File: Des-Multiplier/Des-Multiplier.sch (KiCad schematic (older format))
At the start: 44 parts, among them SW1 SW_Push, U1 NE555P, U2 NE555P

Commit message: added state machine based timing control
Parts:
- added U?: 74LS175, symbol 74xx:74LS175
- added U? (x7): 74HC00, symbol 74xx:74HC00
- added U? (x6): 74LS00, symbol 74xx:74LS00
- C1, C2, C3, C4: symbol Device:C -> Des-Multiplier-rescue:C-Device
- D? (x8): symbol Device:LED -> Des-Multiplier-rescue:LED-Device
- R1, R2, R3, R4, R? (x16): symbol Device:R -> Des-Multiplier-rescue:R-Device
- SW1: symbol Switch:SW_Push -> Des-Multiplier-rescue:SW_Push-Switch
- SW? (x2): symbol Switch:SW_DIP_x04 -> Des-Multiplier-rescue:SW_DIP_x04-Switch
- U1, U2: symbol Timer:NE555P -> Des-Multiplier-rescue:NE555P-Timer
- U? (x3): symbol 74xx:74LS194 -> Des-Multiplier-rescue:74LS194-74xx
- U? (x2): symbol 74xx:74LS283 -> Des-Multiplier-rescue:74LS283-74xx
- U?: symbol 74xx:74LS244 -> Des-Multiplier-rescue:74LS244-74xx
- U?: symbol 74xx:74LS273 -> Des-Multiplier-rescue:74LS273-74xx
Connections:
- net labels added: AccCLK, Acc_Load_En, Load, PreState0, ResetFlag, State0, State1, State2, ~AccCLK, ~GoDetect, ~GoEdge, ~Load, ~Load~, ~Q1~nQ0, ~Q2~n~Q1~, ~Reset, ~ResetFlag, ~S2~nQ0, ~State0, ~State1, ~State2
- net labels removed: Astatus+CLK, Reset
- wire segments 129 -> 152
- no-connect marks 7 -> 8

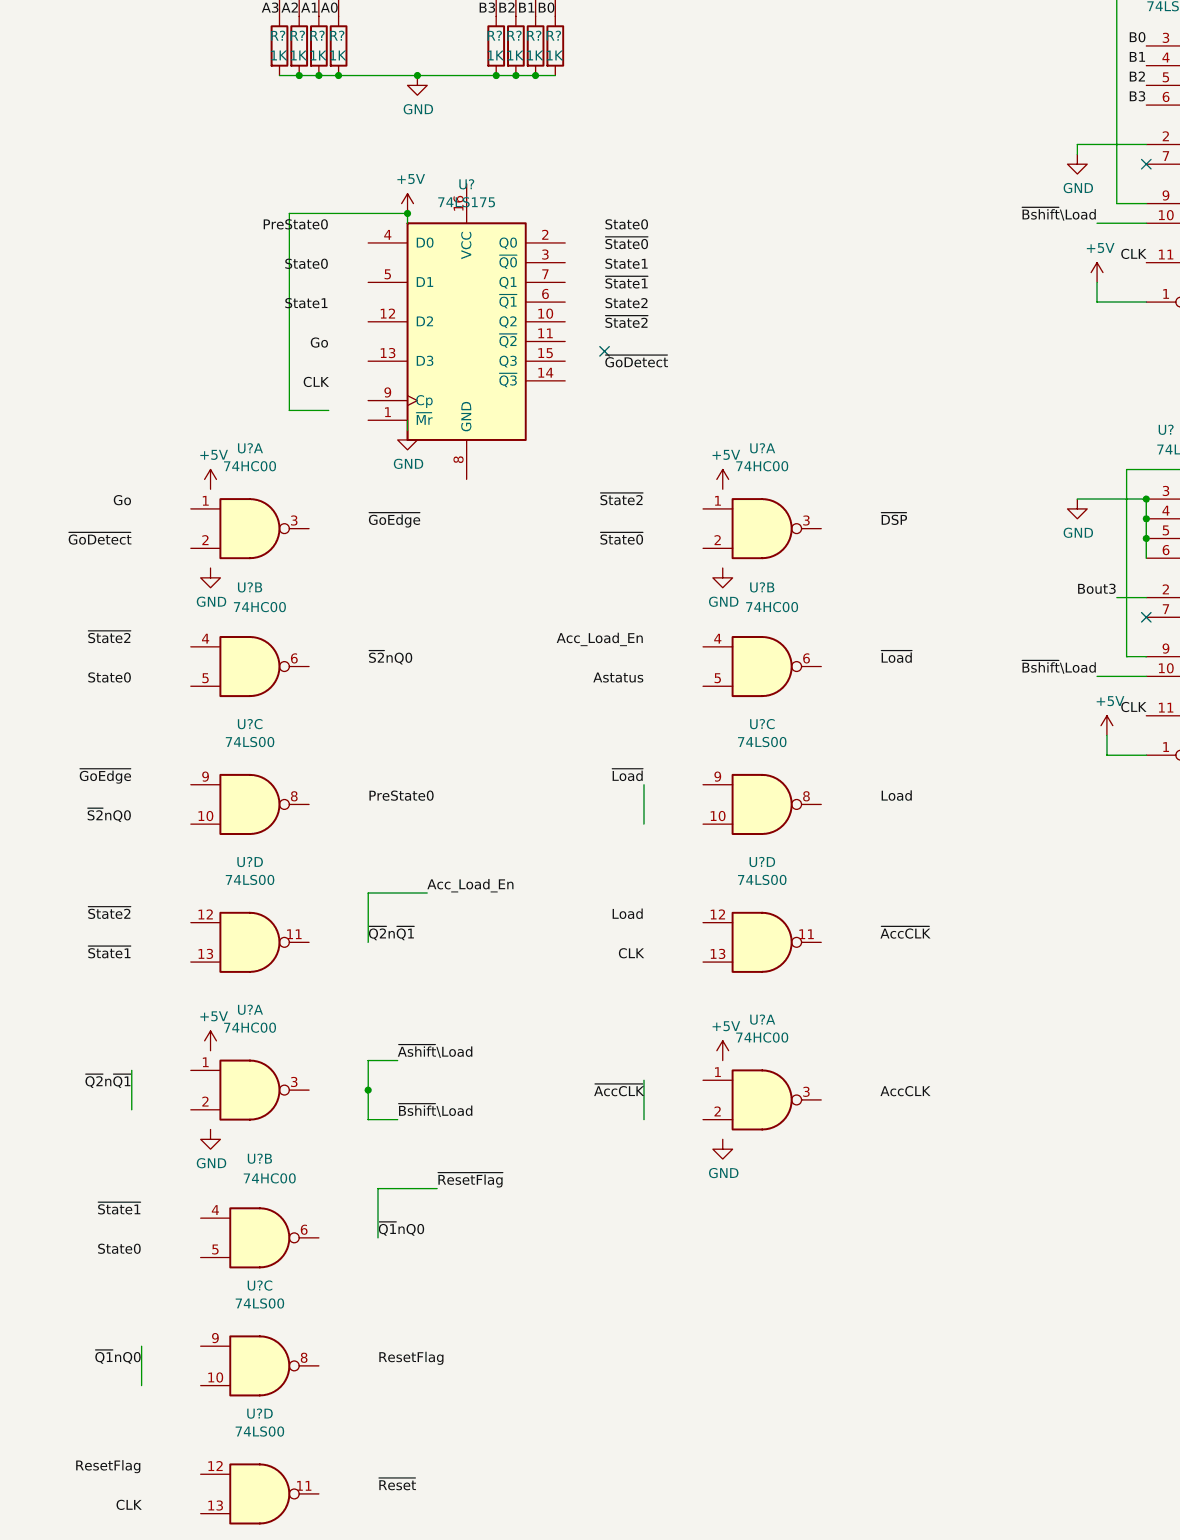
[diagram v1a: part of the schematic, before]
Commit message: updating logic symbols
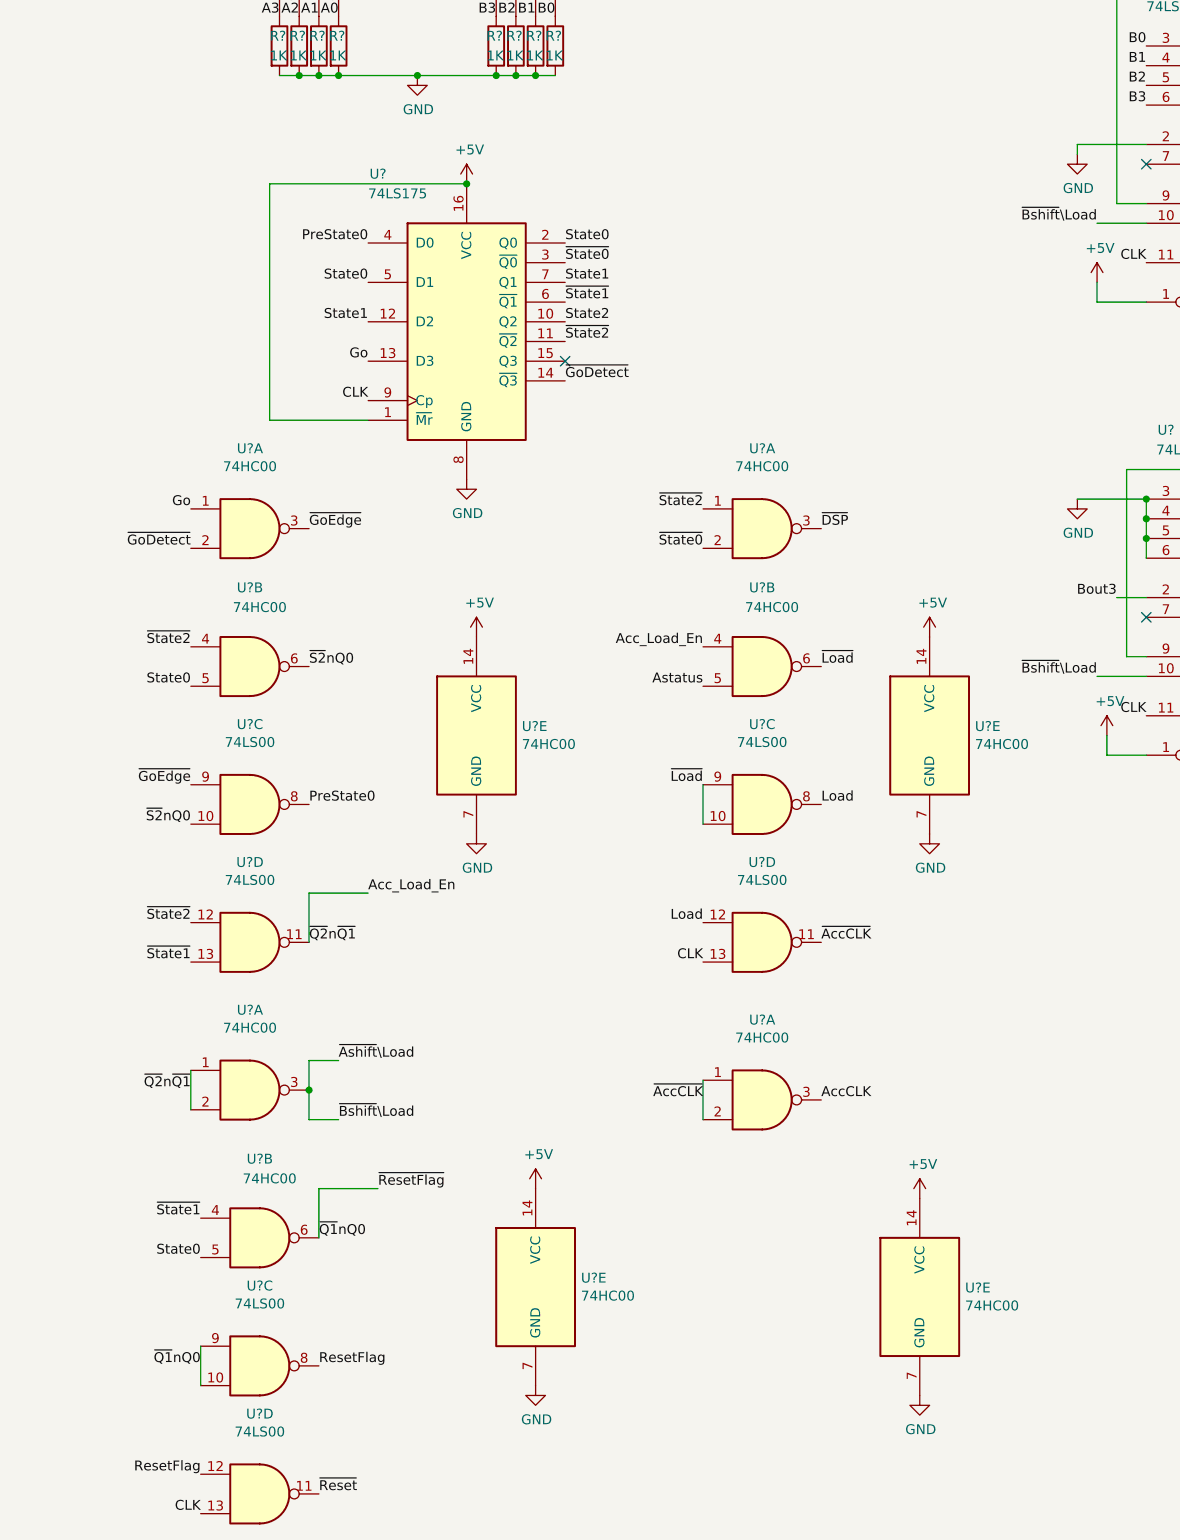
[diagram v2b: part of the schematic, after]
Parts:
- added U? (x4): 74HC00, symbol 74xx:74HC00
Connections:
- wire segments 152 -> 150

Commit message: pcb production beigns
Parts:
- added A1: Arduino_Nano_Every, Module:Arduino_Nano, symbol MCU_Module:Arduino_Nano_Every
- added C5: 10n, Capacitor_THT:C_Disc_D5.0mm_W2.5mm_P2.50mm, symbol Device:C
- D1, D2, D3, D4, D5, D6, D7, D8: renamed from D?; footprint (none) -> LED_THT:LED_D3.0mm
- R10, R11, R12, R13, R14, R15, R16, R17, R18, R19, R20, R5, R6, R7, R8, R9: renamed from R?; footprint (none) -> Resistor_THT:R_Axial_DIN0207_L6.3mm_D2.5mm_P7.62mm_Horizontal
- SW2, SW3: renamed from SW?; footprint (none) -> Package_DIP:DIP-8_W7.62mm
- U10, U11, U13, U14: renamed from U?; footprint (none) -> Package_DIP:DIP-14_W7.62mm
- U10, U11, U13: renamed from U?; value 74LS00 -> 74HC00; footprint (none) -> Package_DIP:DIP-14_W7.62mm
- U10: renamed from U?; value 74LS00 -> 74HC00; footprint (none) -> Package_DIP:DIP-14_W7.62mm; symbol 74xx:74LS00 -> 74xx:74HC00
- U12, U3, U4, U7, U8, U9: renamed from U?; footprint (none) -> Package_DIP:DIP-16_W7.62mm
- U5, U6: renamed from U?; footprint (none) -> Package_DIP:DIP-20_W7.62mm
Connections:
- net +5V: now also A1.30 (VIN)
- net A0: now also A1.13 (D10)
- net A1: now also A1.12 (D9)
- net A2: now also A1.11 (D8)
- net A3: now also A1.10 (D7)
- net AccCLK: now also A1.6 (D3), C5.1
- net B0: now also A1.19 (A0)
- net B1: now also A1.20 (A1)
- net B2: now also A1.21 (A2)
- net B3: now also A1.22 (A3)
- net GND: now also A1.29 (GND), A1.4 (GND), C5.2
- net Go: now also A1.9 (D6)
- net ~Ashift~\Load: now also A1.8 (D5)
- net ~DSP: now also A1.7 (D4)
- net ~Reset: now also A1.5 (D2)
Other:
- note added: "This is used to filter out race pulse\n"

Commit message: pcb layout draft
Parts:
- added J1, J2: Conn_01x04_Male, Connector_PinHeader_2.54mm:PinHeader_1x04_P2.54mm_Vertical, symbol Connector:Conn_01x04_Male
- added J3: Conn_01x08_Male, Connector_PinHeader_2.54mm:PinHeader_1x08_P2.54mm_Vertical, symbol Connector:Conn_01x08_Male
- added J4, J6: Conn_01x02_Male, Connector_PinHeader_2.54mm:PinHeader_1x02_P2.54mm_Vertical, symbol Connector:Conn_01x02_Male
- added J5: R, Resistor_THT:R_Axial_DIN0207_L6.3mm_D2.5mm_P7.62mm_Horizontal, symbol Device:R
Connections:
- net +5V: now also J6.1 (Pin_1)
- net A0: now also J1.1 (Pin_1)
- net A1: now also J1.2 (Pin_2)
- net A2: now also J1.3 (Pin_3)
- net A3: now also J1.4 (Pin_4)
- net B0: now also J2.1 (Pin_1)
- net B1: now also J2.2 (Pin_2)
- net B2: now also J2.3 (Pin_3)
- net B3: now also J2.4 (Pin_4)
- net GND: now also J6.2 (Pin_2)
- net Go: now also J4.1 (Pin_1)
- net ~DSP: now also J4.2 (Pin_2), J5.1, J5.2
- net Out3: now reaches D4.2 (A), U6.12 (O3a)
- net Out3: now also J3.4 (Pin_4)
- net Out2: now reaches D3.2 (A), U6.14 (O2a)
- net Out2: now also J3.3 (Pin_3)
- net Out1: now reaches D2.2 (A), U6.16 (O1a)
- net Out1: now also J3.2 (Pin_2)
- net Out0: now reaches D1.2 (A), U6.18 (O0a)
- net Out0: now also J3.1 (Pin_1)
- net Out7: now reaches D8.2 (A), U6.3 (O3b)
- net Out7: now also J3.8 (Pin_8)
- net Out6: now reaches D7.2 (A), U6.5 (O2b)
- net Out6: now also J3.7 (Pin_7)
- net Out5: now reaches D6.2 (A), U6.7 (O1b)
- net Out5: now also J3.6 (Pin_6)
- net Out4: now reaches D5.2 (A), U6.9 (O0b)
- net Out4: now also J3.5 (Pin_5)
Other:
- moved on the sheet: D1, D2, D3, D4, D5, D6, D7, D8, R18, R19, R20, R5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

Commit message: board changes
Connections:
- net ~DSP: no longer J4.2 (Pin_2), J5.1, U6.1 (OEa), U6.19 (OEb)
- new net ~DSP1: J4.2 (Pin_2), J5.1, U6.1 (OEa), U6.19 (OEb)
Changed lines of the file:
@@
 	11800 4100 11800 4450
 Text Label 11650 4450 2    50   ~ 0
-~DSP
+~DSP1
 $Comp
 L power:GND #PWR0122
@@
 Go
 Text Label 13450 7350 0    50   ~ 0
-~DSP
+~DSP1
 $Comp
 L Device:R J5
@@
 $EndComp
 Text Label 12650 5050 2    50   ~ 0
-~DSP
+~DSP1
 Text Label 12650 5350 3    50   ~ 0
 ~DSP
